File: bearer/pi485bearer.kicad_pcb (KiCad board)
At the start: 2 copper layers, 70 x 30 mm, 23 parts, among them P1 PWR, P2 Rasperry Pi, P3 RO, P4 TERM, P5 CONN_01X04, P6 CONN_01X04, Q1 2N3904, Q2 2N3904, Q3 2N3904, Q4 2N3906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

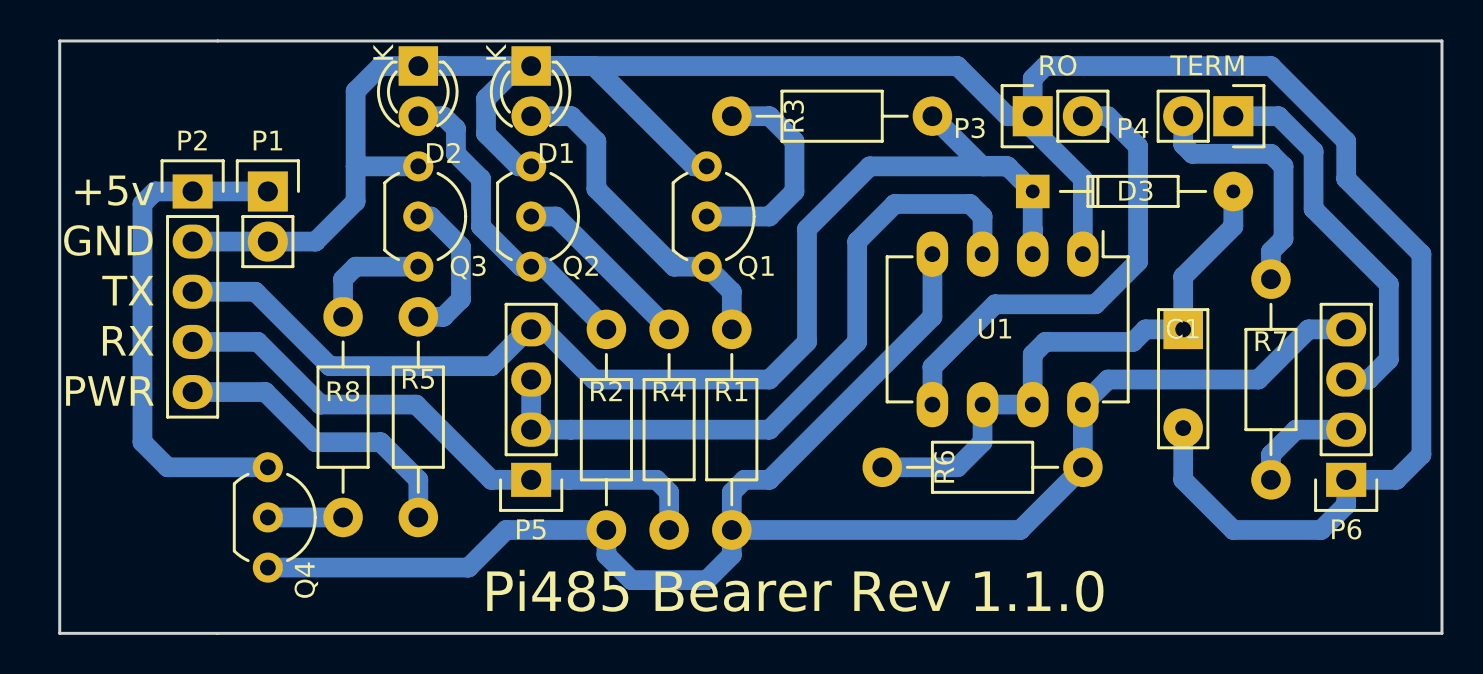
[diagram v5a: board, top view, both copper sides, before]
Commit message: * Found a huge issue with the bearer... where the TX and RX were backwards, due to the header for the module being ... um... reversed. :-/
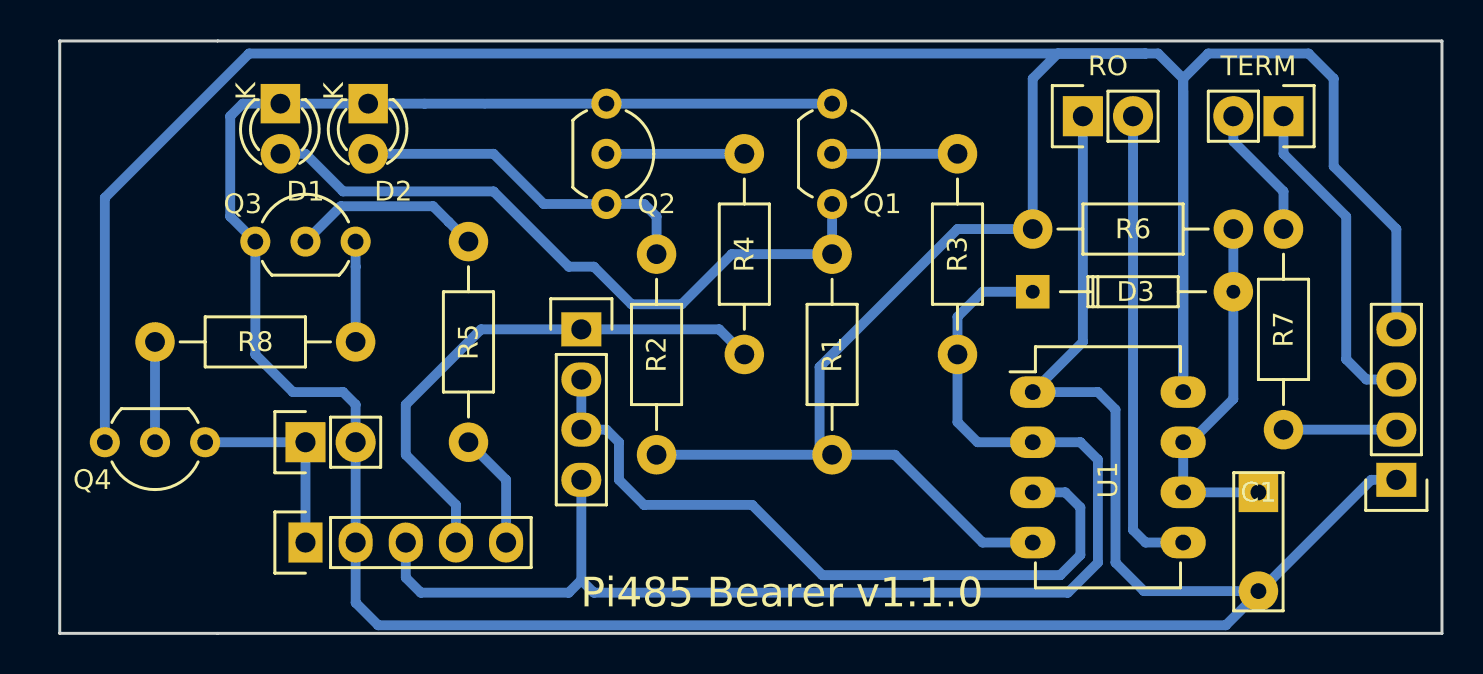
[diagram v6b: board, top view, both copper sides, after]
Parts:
- moved R6 21.5 mm to (88.9, 30.5), turned to 180 degrees
- moved P2 18.7 mm to (41.9, 46.4), turned to 90 degrees
- moved D1 12.8 mm to (40.6, 24.1)
- moved P1 12.8 mm to (41.9, 41.3), turned to 90 degrees
- moved R3 11.6 mm to (74.9, 26.7), turned to 270 degrees
- moved R4 9.67 mm to (64.1, 26.7)
- moved Q3 9.09 mm to (39.4, 31.1), turned to 0 degrees
- moved C1 9.09 mm to (90.2, 43.8)
- moved P5 8.03 mm to (55.9, 35.6), turned to 270 degrees
- moved U1 7.43 mm to (78.7, 38.7), turned to 0 degrees
- moved Q1 7.10 mm to (68.6, 24.1)
- moved R1 6.35 mm to (68.6, 31.8)
- moved D3 5.08 mm to (78.7, 33.7)
- moved Q2 4.96 mm to (57.1, 24.1)
- moved R2 4.58 mm to (59.7, 31.8)
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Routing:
- net /lctec485/VCIN: track 85.0 -> 193.1 mm
- net Net-(D1-Pad2): track 17.2 -> 34.7 mm
- net VCC: track 25.6 -> 10.2 mm
- net GND: track 137.4 -> 150.9 mm
- net Net-(C1-Pad1): track 28.8 -> 18.4 mm
- net /(485PWR)_GPIO18: track 15.2 -> 5.87 mm
- net Net-(P4-Pad2): track 13.0 -> 6.77 mm
- net Net-(Q1-Pad2): track 11.2 -> 6.35 mm
- net /lctec485/B: track 19.5 -> 16.6 mm
- net /(TXDO)_GPIO14: track 63.6 -> 66.2 mm
- net Net-(Q2-Pad2): track 9.35 -> 6.99 mm
- net /lctec485/DE: track 35.3 -> 37.5 mm
- net /(RXDO)_GPIO15: track 29.3 -> 27.3 mm
- net Net-(Q3-Pad2): track 7.98 -> 9.74 mm
- net Net-(D2-Pad2): track 16.2 -> 17.8 mm
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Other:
- net class Default: clearance 0.2 -> 0.25; trace_width 1 -> 0.5
- rule trace_clearance: 0.2 -> 0.25
- rule trace_min: 0.8 -> 0.5
- board text added: "Pi485 Bearer v1.1.0"
- board text removed: "+5v"
- board text removed: "GND"
- board text removed: "PWR"
- board text removed: "Pi485 Bearer Rev 1.1.0"
- board text removed: "RX"
- board text removed: "TX"

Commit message: * Re-placed & routed the bearer, now with the headers in the proper orientation. *facepalm*
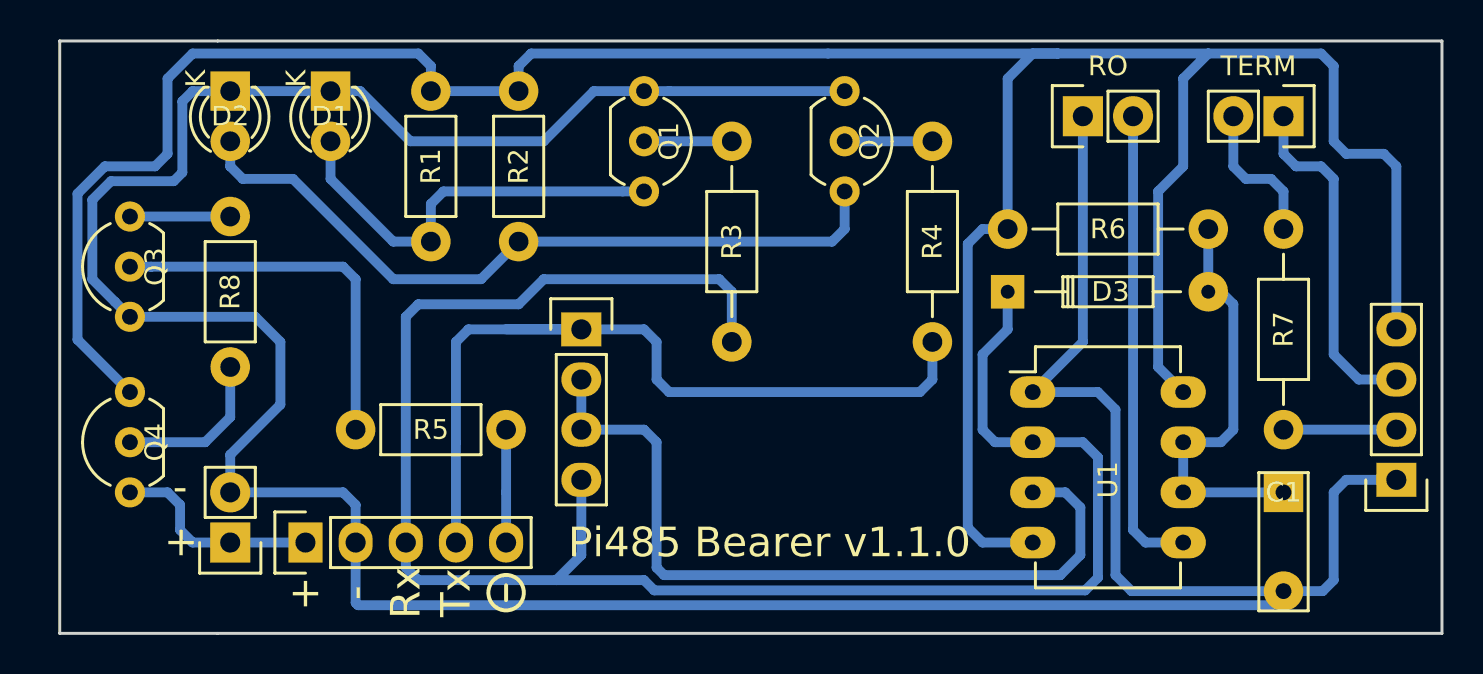
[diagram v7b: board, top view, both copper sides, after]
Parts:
- R1, R2, R5, R8: footprint Resistors_THT:Resistor_Horizontal_RM10mm -> Resistors_THT:Resistor_Horizontal_RM7mm
- moved R1 20.3 mm to (48.3, 31.1), turned to 90 degrees
- moved Q2 12.1 mm to (69.2, 23.5)
- moved R3 11.4 mm to (63.5, 26.0)
- moved Q1 9.55 mm to (59.1, 23.5)
- moved R4 9.55 mm to (73.7, 26.0)
- moved R8 8.98 mm to (38.1, 29.8), turned to 270 degrees
- moved Q3 7.41 mm to (33.0, 34.9), turned to 90 degrees
- moved D2 7.01 mm to (38.1, 23.5)
- moved R2 7.01 mm to (52.7, 31.1), turned to 90 degrees
- moved P1 6.35 mm to (38.1, 46.4), turned to 180 degrees
- moved Q4 4.58 mm to (33.0, 43.8), turned to 90 degrees
- moved D1 2.62 mm to (43.2, 23.5)
- moved R5 2.01 mm to (52.1, 40.6), turned to 180 degrees
- moved R6 1.27 mm to (87.6, 30.5)
- moved C1 1.27 mm to (91.4, 43.8)
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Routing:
- net /lctec485/VCIN: track 193.1 -> 148.7 mm
- net /(TXDO)_GPIO14: track 66.2 -> 94.2 mm
- net GND: track 150.9 -> 174.4 mm
- net Net-(D2-Pad2): track 17.8 -> 37.7 mm
- net /(RXDO)_GPIO15: track 27.3 -> 43.0 mm
- net Net-(D1-Pad2): track 34.7 -> 21.3 mm
- net Net-(Q3-Pad2): track 9.74 -> 19.3 mm
- net Net-(C1-Pad1): track 18.4 -> 21.5 mm
- net Net-(Q4-Pad2): track 5.08 -> 8.15 mm
- net /lctec485/DE: track 37.5 -> 40.1 mm
- net Net-(Q2-Pad2): track 6.99 -> 4.44 mm
- net Net-(Q1-Pad2): track 6.35 -> 4.45 mm
- net /lctec485/B: track 16.6 -> 17.6 mm
- net Net-(P4-Pad2): track 6.77 -> 7.51 mm
- net VCC: track 10.2 -> 10.7 mm
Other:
- board text added: "+"
- board text added: "-"
- board text added: "Rx"
- board text added: "Tx"
